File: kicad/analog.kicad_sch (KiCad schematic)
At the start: 35 parts, among them J25 pH probe, J26 pH module, J27 AIN3, U10 TL431BCDBZR, U5 B0505S-1WR3, U6 AMS1117-3.3, U7 ISO1540DR, U8 ADS1115IDGSR, U9 TLV9062IDR

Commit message: kicad: simpler non-isolated pH amplifier after review of the hand-built setup
Nothing in the tank is grounded and ~0.1 pH stability is enough, so the
galvanic isolation (B0505S + ISO1540) and the TL431 reference go. The
on-board pH amplifier now mirrors the proven PH-4502C mod: 10 MOhm +
6.8 nF styroflex input filter, TLV9062 buffer, bias 3V3/2 buffered,
plus 1 MOhm in the reference line as ground-loop insurance. AIN2 is a
module input for 5 V amplifier boards with a 10k/20k divider (0..5 V).
BOM, README and cost (~41 EUR/board at 5, ~33 at 10) updated.

Co-Authored-By: Claude Opus 5.5 <noreply@anthropic.com>
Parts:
- removed C20, C24: 10u, Capacitor_SMD:C_0805_2012Metric, symbol Device:C
- removed C21: 2n2 styroflex, Capacitor_THT:C_Axial_L12.0mm_D6.5mm_P15.00mm_Horizontal, symbol Device:C
- removed C22, C23, C25: 100n, Capacitor_SMD:C_0805_2012Metric, symbol Device:C
- removed R53: 10k, Resistor_SMD:R_0805_2012Metric, symbol Device:R
- removed R54: 1k, Resistor_SMD:R_0805_2012Metric, symbol Device:R
- removed U10: TL431BCDBZR, Package_TO_SOT_SMD:SOT-23, symbol Reference_Voltage:TL431DBZ
- removed U5: B0505S-1WR3, Converter_DCDC:Converter_DCDC_Murata_CRE1xxxxxxSC_THT, symbol Converter_DCDC_Isolated:CRE1S0505SC
- removed U6: AMS1117-3.3, Package_TO_SOT_SMD:SOT-223-3_TabPin2, symbol Regulator_Linear:AMS1117-3.3
- removed U7: ISO1540DR, Package_SO:SOIC-8_3.9x4.9mm_P1.27mm, symbol Isolator:ISO1540
- removed U8: ADS1115IDGSR, Package_SO:TSSOP-10_3x3mm_P0.5mm, symbol Analog_ADC:ADS1115IDGS
- removed U9: TLV9062IDR, Package_SO:SOIC-8_3.9x4.9mm_P1.27mm, symbol Amplifier_Operational:TLV9062xD
- added U5: ADS1115IDGSR, Package_SO:TSSOP-10_3x3mm_P0.5mm, symbol Analog_ADC:ADS1115IDGS
- added U6: TLV9062IDR, Package_SO:SOIC-8_3.9x4.9mm_P1.27mm, symbol Amplifier_Operational:TLV9062xD
- C13, C16: value 10u -> 100n; LCSC C15850 -> C49678
- C14: value 10u -> 6n8 styroflex; footprint Capacitor_SMD:C_0805_2012Metric -> Capacitor_THT:C_Axial_L12.0mm_D6.5mm_P15.00mm_Horizontal; LCSC C15850 -> (none); Reichelt (none) -> STYROFLEX 6,8N
- C18: value 100n -> 10u; LCSC C49678 -> C15850
- J26: value pH module -> Module
- R45: value 1k -> 10M; LCSC C17513 -> C26108
- R46, R47: value 4k7 -> 10k; LCSC C17673 -> C17414
- R48: value 220k -> 10k; LCSC C17556 -> C17414
- R49: value 10k -> 1M; LCSC C17414 -> C17514
- R50: value 470 -> 10k; LCSC C17710 -> C17414
- R51: value 10k -> 20k; LCSC C17414 -> C4328
- R52: value 10k -> 1k; LCSC C17414 -> C17513
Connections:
- net ISO_SCL is gone; now on net PH_MID: R47.2
- net ISO_SDA is gone; now on net PH_SIG: R46.2
- net VREF25 is gone; now on net AIN2: R50.2, R51.1
- net +3V3: now also C13.1, C17.1, D27.2 (K), D28.2 (K), J27.1 (Pin_1), JP4.3 (B), R47.1, U5.8 (VDD), U6.8 (V+); no longer C18.1
- net +5V: now also J26.1 (Pin_1); no longer C13.1
- net ADS_ADDR: now also U5.1 (ADDR)
- net AIN2: now also C18.1, U5.6 (AIN2)
- net AIN3: now also C19.1, R52.2, U5.7 (AIN3)
- net AIN3_T: now also R52.1
- net GND: now also C15.2, C16.2, C17.2, C19.2, D27.1 (A), D28.1 (A), J26.3 (Pin_3), J27.3 (Pin_3), JP4.1 (A), R48.2, R51.2, U5.3 (GND), U6.4 (V-)
- net GPIO2_SDA: now also U5.9 (SDA)
- net GPIO3_SCL: now also U5.10 (SCL)
- net PHM_T: now also R50.1
- net PH_BNC: now also R45.1; no longer R48.1
- net PH_BUF: now also R46.1, U6.1, U6.2 (-); no longer R49.1
- net PH_IN: now also C14.1, R45.2, U6.3 (+); no longer R48.2
- net PH_MID: now also C16.1, R48.1, U6.5 (+); no longer R51.2, R52.1
- net PH_REF: now also R49.1, U5.5 (AIN1), U6.6 (-), U6.7; no longer J25.2 (Ext)
- net PH_SIG: now also C15.1, U5.4 (AIN0); no longer R49.2
- removed net ISO_3V3: C16.1, C17.1, C19.1, D27.2 (K), D28.2 (K), J27.1 (Pin_1), JP4.3 (B), R46.1, R47.1, R50.1
- removed net ISO_5V: C14.1, C15.1, J26.1 (Pin_1), R45.1
- removed net ISO_GND: C14.2, C15.2, C16.2, C17.2, C19.2, D27.1 (A), D28.1 (A), J26.3 (Pin_3), J27.3 (Pin_3), JP4.1 (A), R45.2, R52.2
- new net PH_SHELL: C14.2, J25.2 (Ext), R49.2
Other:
- note added: "1M in the reference line: if the tank water ever gets a DC path to GND (grounded sensor), the current through the reference electrode stays below ~1.7 uA instead of mA. The reading then goes visibly wrong, the probe survives. Normal operation: only pA flow, no measurable drop."
- note added: "ADS1115 on 3.3 V (I2C levels match the Pi), address 0x48 (JP 1-2, default) or 0x49 (2-3). All channels are read single-ended (aquaPi driver): AIN0 on-board pH, AIN1 pH bias (monitor, allows AIN0-AIN1 differential later), AIN2 module input (0..5 V via divider), AIN3 general 0..3.3 V."
- note added: "AIN2: module input for amplifier boards (e.g. PH-4502C, ORP) on 5 V. Terminal +5V / SIG / GND. Divider 10k/20k (fitted by default) maps 0..5 V to 0..3.33 V; leave 20k off for 1:1 up to 3.3 V. With 10u: about 2.4 Hz low-pass. Clamped to 0..3.3 V."
- note added: "AIN3: general 0..3.3 V input, 1k + 100n low-pass, clamped. Terminal: 3V3 / AIN3 / GND."
- note added: "Input filter 10M / 6n8 styroflex (68 ms; with the electrode 100M..1G: 0.7..7 s) against pump 50 Hz, second filter 10k/10u after the buffer. Probe load: TLV9062 input only (0.5 pA typ) plus styroflex leakage - no ceramic cap or clamp on PH_BNC/PH_IN. LAYOUT: guard ring (both layers) around PH_BNC, 10M, styroflex lead and TLV9062 pin 3, on net PH_BUF; milled slots around BNC centre pad; short node;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"
- note added: "On-board pH amplifier (like the PH-4502C with low-leakage input). Glass electrode on BNC centre, reference on BNC shell. Probe biased to PH_REF = 1.65 V (3V3 / 2, buffered), AIN0 reads 1.65 V +/- 59 mV/pH; aquaPi's ScaleAux calibration removes offset and slope."
- note removed: "1W isolated DC/DC, 1 kV. 1k dummy load (5 mA) plus LDO quiescent current keep its output from rising at light load. ISO_5V also supplies the external pH module terminal."
- note removed: "ADS1115 on ISO_3V3, I2C address 0x48 (JP 1-2, default) or 0x49 (2-3). ALERT/RDY unused. All channels are read single-ended (aquaPi driver): AIN0 on-board pH, AIN1 pH reference (monitor, allows AIN0-AIN1 differential later), AIN2 external pH amplifier module, AIN3 general."
- note removed: "AIN2: external pH amplifier module (probe kit board), terminal ISO_5V / SIG / ISO_GND - isolated as well. Output (about 2.5 V at pH 7) filtered 10k/10u (1.6 Hz) and clamped to 0..3.3 V."
- note removed: "AIN3: general 0..3.3 V input on the isolated side (sensor GND must be ISO_GND!), 1k + 100n, clamped. Terminal: ISO_3V3 / AIN3 / ISO_GND."
- note removed: "ISO1540: side 2 (normal low level) on the Pi I2C bus; side 1 (low level 0.57..0.8 V) only drives the ADS1115 (V_IL 0.99 V at 3.3 V). Side-1 pull-ups 4k7 -> 0.7 mA, within the required 0.5..3.5 mA."
- note removed: "On-board pH front end: glass electrode on BNC centre, reference on BNC shell. The probe is biased to PH_REF = 1.25 V (TL431 2.495 V / 2), so AIN0 reads 1.25 V +/- 59 mV/pH single-ended; aquaPi's 2-point calibration removes the offset. BNC shell pads must stay on PH_REF, NOT GND."
- note removed: "Probe load: TLV9062 input (0.5 pA typ) and the polystyrene (styroflex) filter cap across the probe; no ceramic cap or clamp on PH_BNC/PH_IN (leakage). Cap x electrode R (100M..1G): 0.2..2 s input filter; swap for 47p..6n8 as needed. Second 50 Hz filter after the buffer: 10k/10u, 1.6 Hz. LAYOUT: guard ring around PH_BNC, R/C input parts and TLV9062 pin 3, connected to PH_BUF; slots; clean flux."
- note removed: "TL431B (TI, DBZ pinout 1=K 2=REF 3=A; TL432 differs!), ~1.6 mA via 470R. Divided and buffered to PH_REF = 1.25 V, which also drives the probe reference electrode."
- note removed: "The whole analog section is galvanically isolated (ISO_GND). The tank water is often tied to board GND through other sensors (e.g. a DS18B20 sleeve); without isolation a DC current would flow through the pH reference electrode and destroy it. LAYOUT: keep >= 2 mm (better a slot) between the GND and ISO_GND domains; only the B0505S DC/DC and the ISO1540 cross the gap."
- title: aquaPCB – Isolated ADC and pH front end -> aquaPCB – ADS1115 ADC and pH amplifier

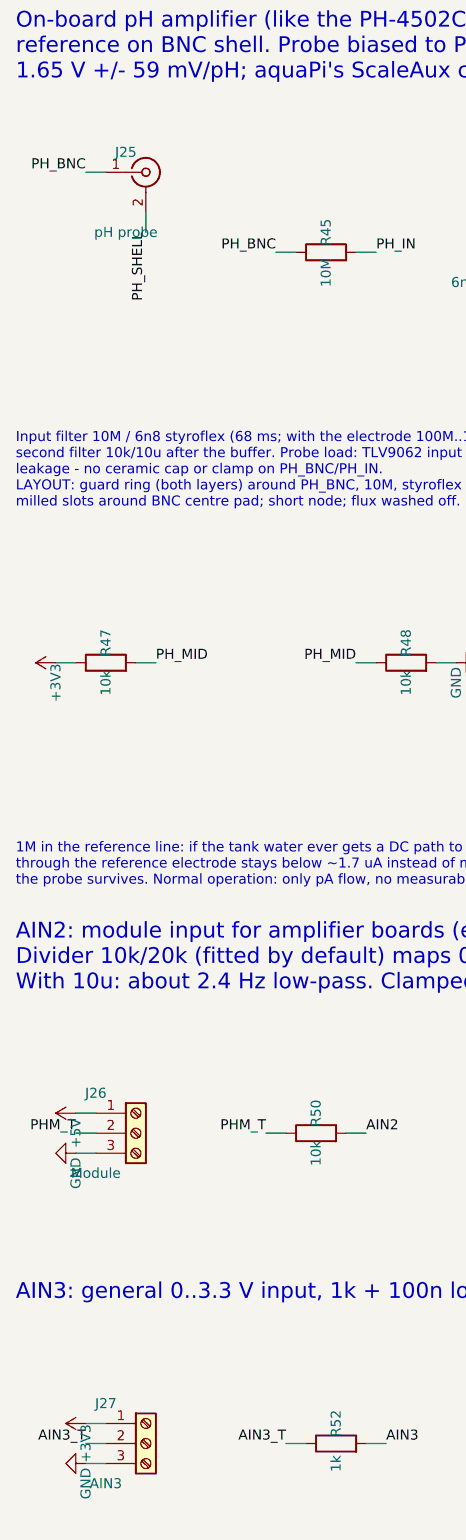
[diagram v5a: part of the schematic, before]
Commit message: kicad: drop the third 1-Wire terminal
Two terminals are enough for the bus (several sensors per terminal).
Saves one AKL 101-03 (0.39 EUR/board) and board edge space.

Co-Authored-By: Claude Opus 5.5 <noreply@anthropic.com>
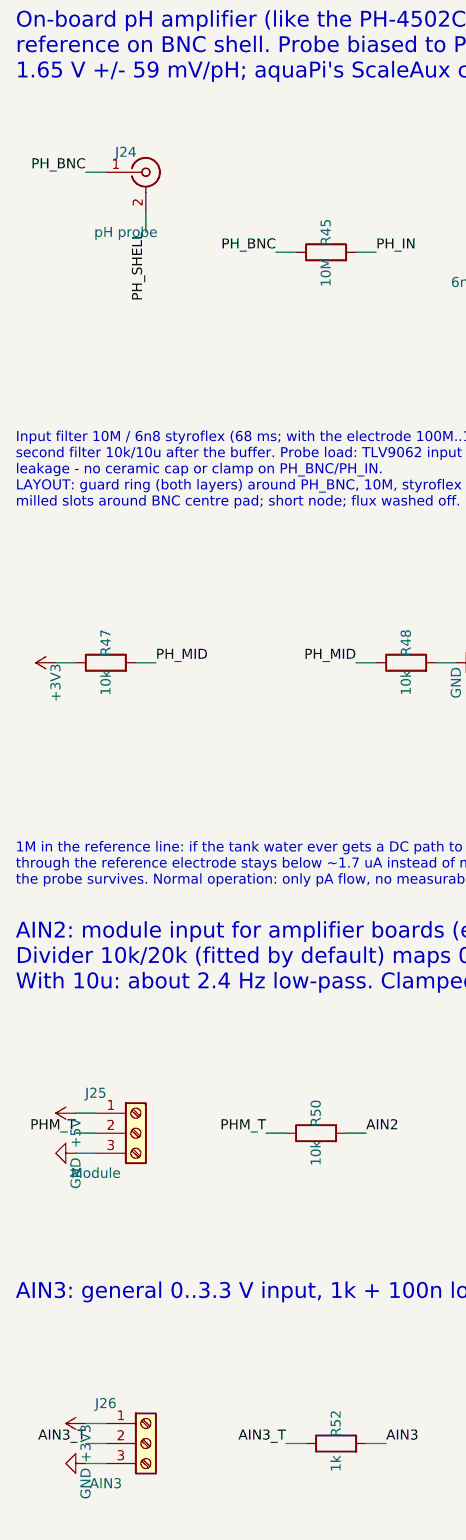
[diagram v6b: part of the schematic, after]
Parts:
- removed J25: pH probe, Connector_Coaxial:BNC_Amphenol_031-5539_Vertical, symbol Connector:Conn_Coaxial
- removed J27: AIN3, TerminalBlock_Phoenix:TerminalBlock_Phoenix_MKDS-1,5-3-5.08_1x03_P5.08mm_Horizontal, symbol Connector:Screw_Terminal_01x03
- added J24: pH probe, Connector_Coaxial:BNC_Amphenol_031-5539_Vertical, symbol Connector:Conn_Coaxial
- added J25: Module, TerminalBlock_Phoenix:TerminalBlock_Phoenix_MKDS-1,5-3-5.08_1x03_P5.08mm_Horizontal, symbol Connector:Screw_Terminal_01x03
- J26: value Module -> AIN3
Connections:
- net +3V3: now also J26.1 (Pin_1)
- net +5V: now also J25.1 (Pin_1); no longer J26.1 (Pin_1)
- net AIN3_T: now also J26.2 (Pin_2)
- net GND: now also J25.3 (Pin_3)
- net PHM_T: now also J25.2 (Pin_2); no longer J26.2 (Pin_2)
- net PH_BNC: now also J24.1 (In)
- net PH_SHELL: now also J24.2 (Ext)

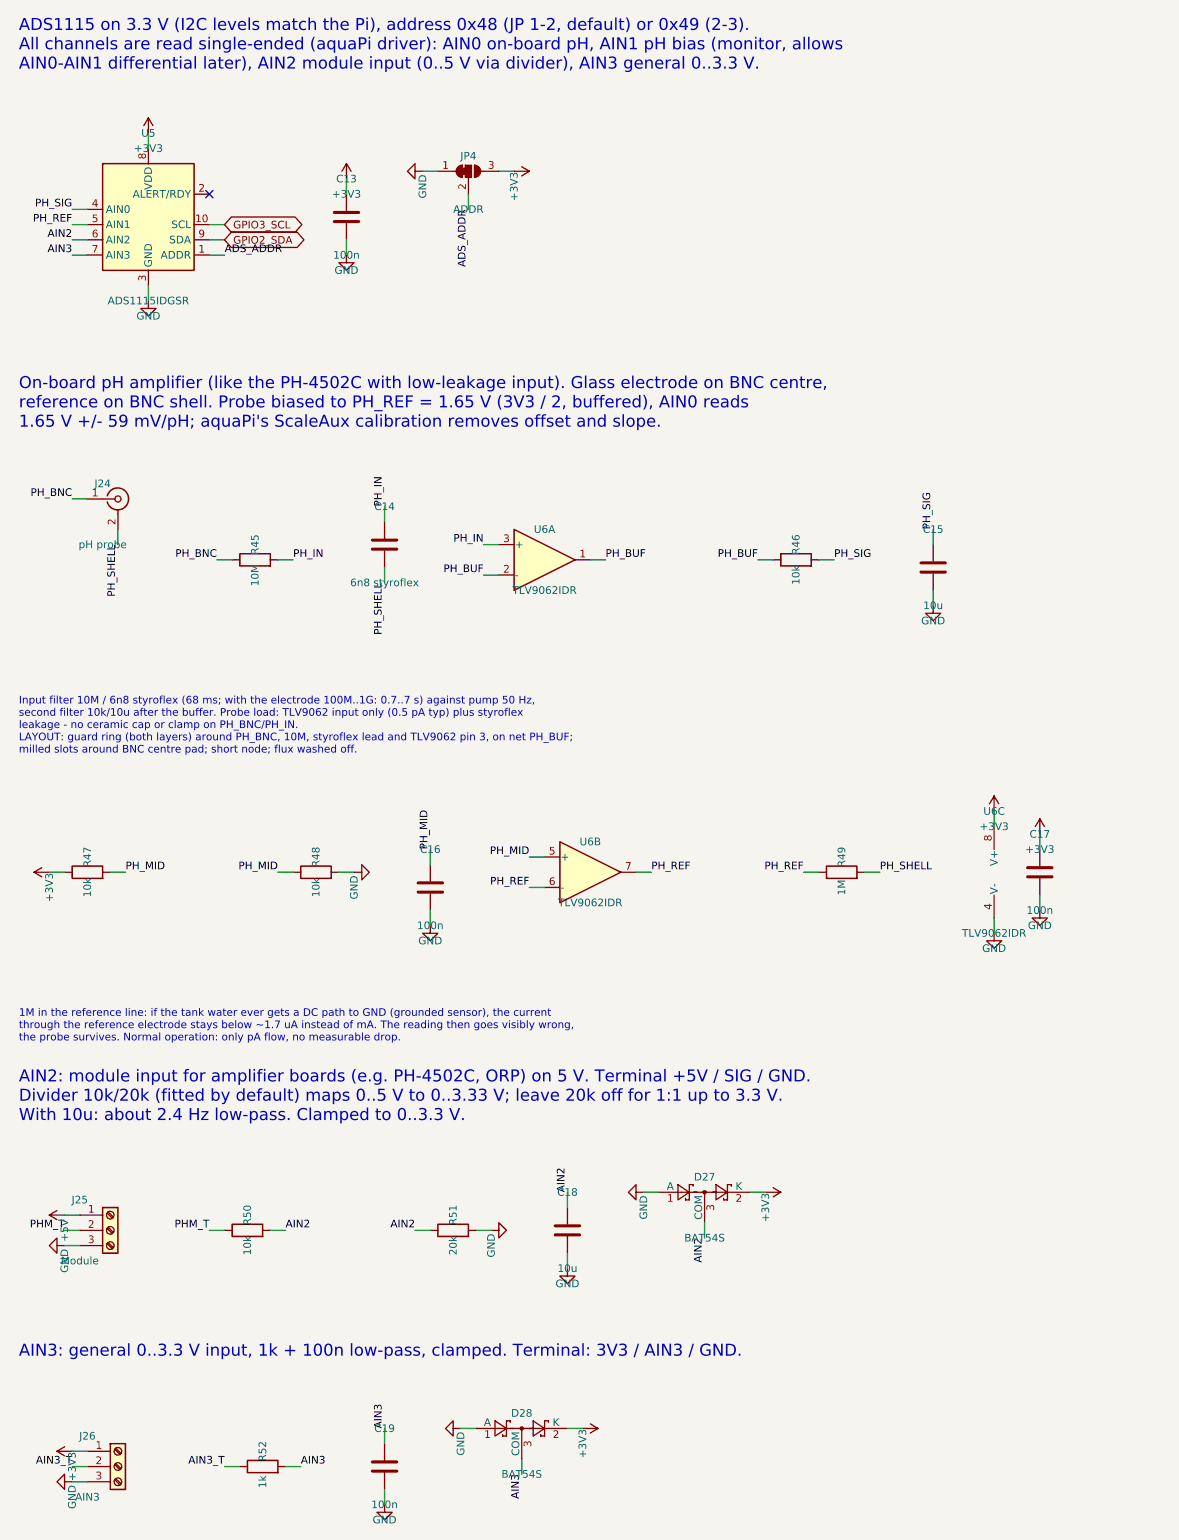
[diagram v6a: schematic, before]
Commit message: kicad: restore the hand-edited schematic from KiCad local history
f617249 overwrote the schematic that had been tidied by hand in
eeschema (labels replaced by wires and junctions) with a regenerated
draft and new symbol UUIDs. Restore all sheets and the project file
from KiCad's local history snapshot eb84d42 (2026-09-30 14:45).
Connectivity matches that snapshot; all 153 symbols link to the
footprints in aquaPCB.kicad_pcb again. The third 1-Wire terminal (J21)
is still in the schematic and has to be deleted in eeschema.

Co-Authored-By: Claude Opus 5.5 <noreply@anthropic.com>
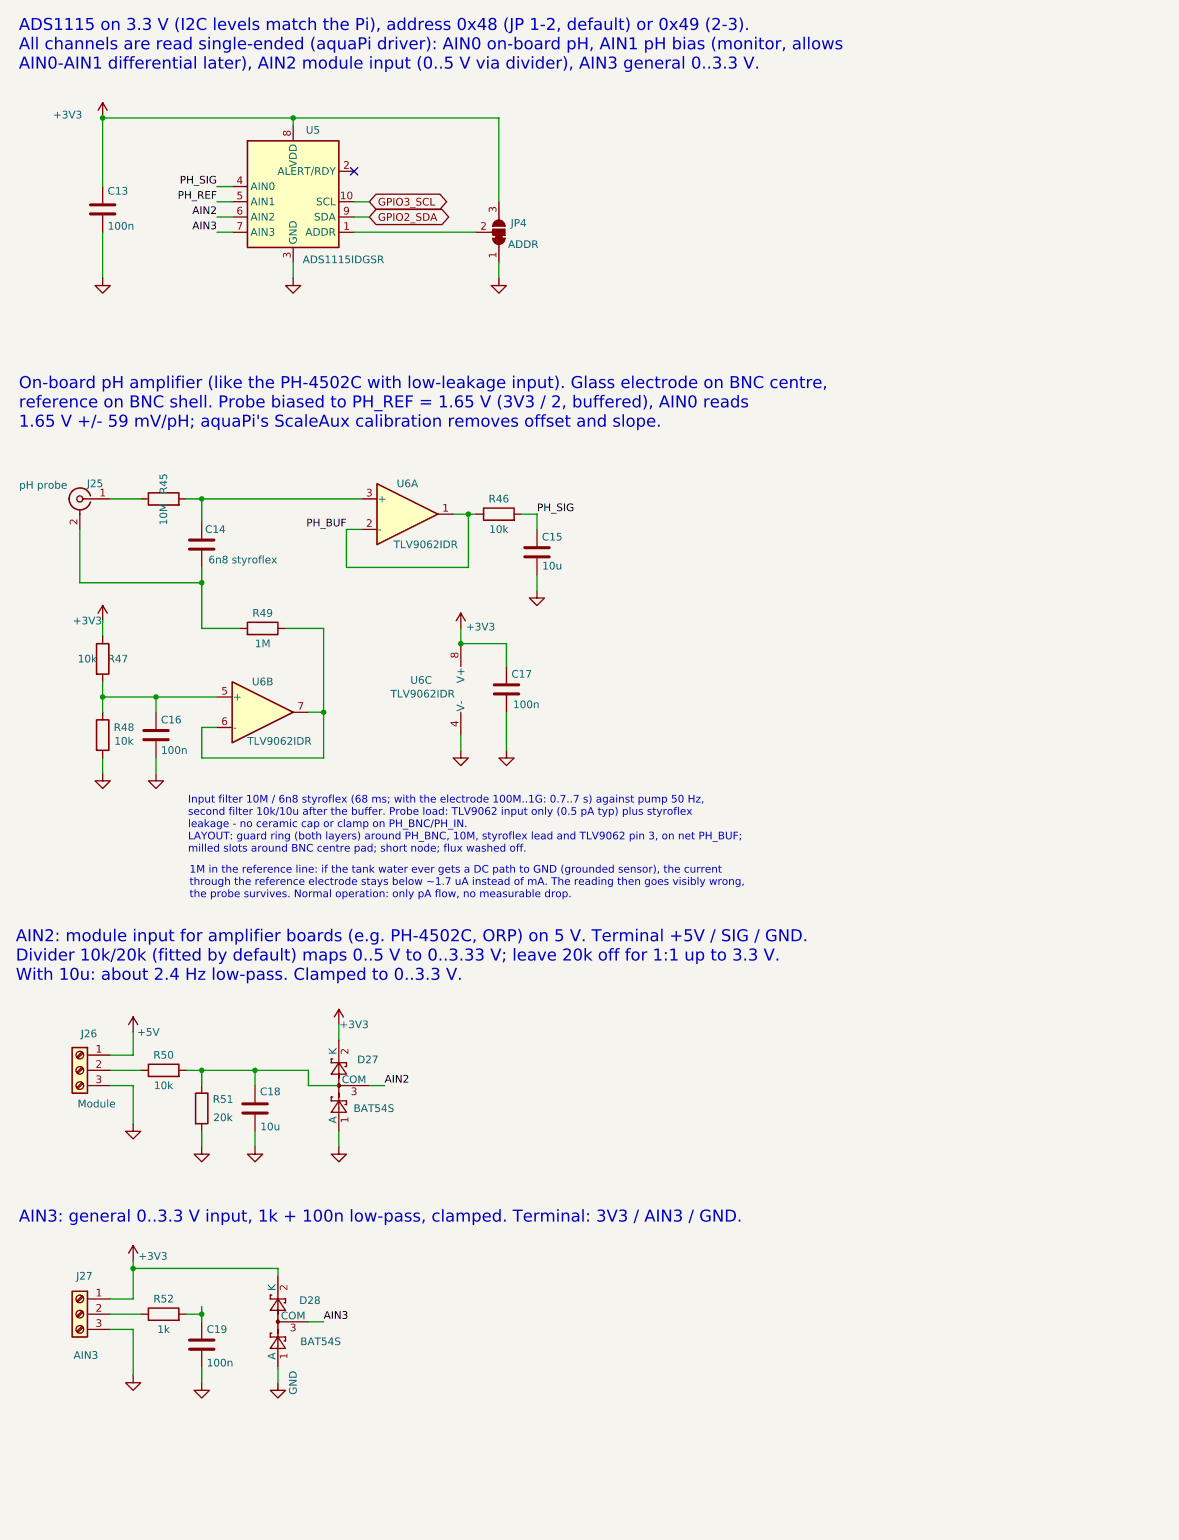
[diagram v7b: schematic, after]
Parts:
- removed J24: pH probe, Connector_Coaxial:BNC_Amphenol_031-5539_Vertical, symbol Connector:Conn_Coaxial
- removed J25: Module, TerminalBlock_Phoenix:TerminalBlock_Phoenix_MKDS-1,5-3-5.08_1x03_P5.08mm_Horizontal, symbol Connector:Screw_Terminal_01x03
- added J25: pH probe, Connector_Coaxial:BNC_Amphenol_031-5539_Vertical, symbol Connector:Conn_Coaxial
- added J27: AIN3, TerminalBlock_Phoenix:TerminalBlock_Phoenix_MKDS-1,5-3-5.08_1x03_P5.08mm_Horizontal, symbol Connector:Screw_Terminal_01x03
- J26: value AIN3 -> Module
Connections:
- net PHM_T is gone; now on an unnamed net: R50.1
- net +3V3: now also J27.1 (Pin_1); no longer J26.1 (Pin_1)
- net +5V: now also J26.1 (Pin_1)
- net AIN2: no longer C18.1, R50.2, R51.1
- net AIN3: no longer C19.1, R52.2
- net GND: now also J27.3 (Pin_3)
- net PH_REF: no longer R49.1, U6.6 (-), U6.7
- net ADS_ADDR: no longer names the net of JP4.2 (C), U5.1 (ADDR)
- net AIN3_T: no longer names the net of J26.2 (Pin_2)
- net AIN3_T: no longer R52.1
- net PH_BNC: no longer names the net of R45.1
- net PH_BNC: now also J25.1 (In)
- net PH_IN: no longer names the net of C14.1, R45.2, U6.3 (+)
- net PH_MID: no longer names the net of C16.1, R47.2, R48.1, U6.5 (+)
- net PH_SHELL: no longer names the net of C14.2, R49.2
- net PH_SHELL: now also J25.2 (Ext)
- new net: R49.1, U6.6 (-), U6.7
- new net: C18.1, R50.2, R51.1
- new net: J27.2 (Pin_2), R52.1
- new net: C19.1, R52.2

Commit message: kicad: fix connections broken while tidying the schematic
analog: AIN1 (U5.5) reconnected to PH_REF, AIN2 and AIN3 filter nodes
reconnected to their clamps / ADC inputs (net labels), two dangling
wire pieces removed. power: seven dangling wire stubs removed.
ERC clean; connectivity equals the design of 7b8e8dd except the removed
J21 and the (equivalent) swapped JP3 pins. Minimal text edits, the rest
of the hand-edited drawing is untouched.

Co-Authored-By: Claude Opus 5.5 <noreply@anthropic.com>
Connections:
- net AIN2: now also C18.1, R50.2, R51.1
- net AIN3: now also C19.1, R52.2
- net PH_REF: now also R49.1, U6.6 (-), U6.7
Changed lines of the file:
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@@
 	(wire
 		(pts
-			(xy 73.66 208.28) (xy 73.66 205.74)
-		)
-		(stroke
-			(width 0)
-			(type default)
-		)
-	)
-	(wire
-		(pts
 			(xy 111.76 115.57) (xy 111.76 113.03)
 		)
@@
 	(wire
 		(pts
-			(xy 78.74 208.28) (xy 73.66 208.28)
-		)
-		(stroke
-			(width 0)
-			(type default)
-		)
-	)
-	(wire
-		(pts
 			(xy 73.66 146.05) (xy 76.2 146.05)
 		)
@@
 		)
 	)
+	(label "PH_REF"
+		(at 76.2 139.7 0)
+		(effects
+			(font
+				(size 1.27 1.27)
+			)
+			(justify left bottom)
+		)
+	)
+	(label "AIN2"
+		(at 73.66 205.74 0)
+		(effects
+			(font
+				(size 1.27 1.27)
+			)
+			(justify left bottom)
+		)
+	)
+	(label "AIN3"
+		(at 55.88 245.11 90)
+		(effects
+			(font
+				(size 1.27 1.27)
+			)
+			(justify left bottom)
+		)
+	)
